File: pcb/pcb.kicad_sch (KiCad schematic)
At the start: 23 parts, among them SW1 SW_Push, SW10 SW_Push, SW11 SW_Push, SW12 SW_Push, SW13 SW_Push, SW14 SW_Push, SW15 SW_Push, SW16 SW_Push, SW17 SW_Push, SW18 SW_Push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

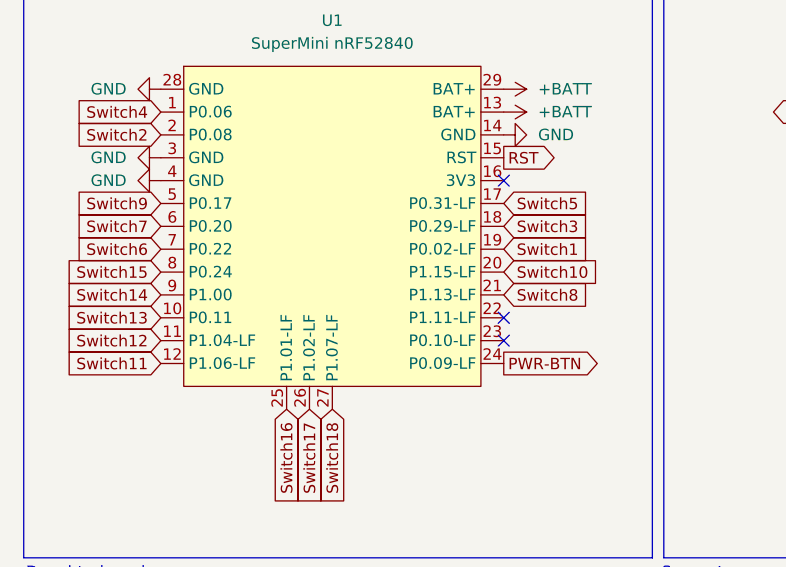
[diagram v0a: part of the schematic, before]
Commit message: feat: new hotswap footprint + routing
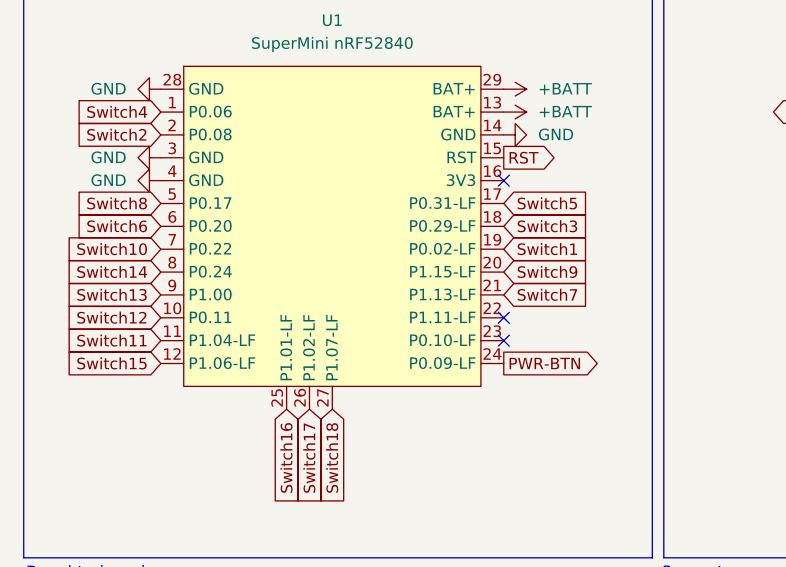
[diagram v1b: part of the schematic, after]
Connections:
- net Switch10: now also U1.7 (P0.22); no longer U1.20 (P1.15-LF)
- net Switch11: now also U1.11 (P1.04-LF); no longer U1.12 (P1.06-LF)
- net Switch12: now also U1.10 (P0.11); no longer U1.11 (P1.04-LF)
- net Switch13: now also U1.9 (P1.00); no longer U1.10 (P0.11)
- net Switch14: now also U1.8 (P0.24); no longer U1.9 (P1.00)
- net Switch15: now also U1.12 (P1.06-LF); no longer U1.8 (P0.24)
- net Switch6: now also U1.6 (P0.20); no longer U1.7 (P0.22)
- net Switch7: now also U1.21 (P1.13-LF); no longer U1.6 (P0.20)
- net Switch8: now also U1.5 (P0.17); no longer U1.21 (P1.13-LF)
- net Switch9: now also U1.20 (P1.15-LF); no longer U1.5 (P0.17)
